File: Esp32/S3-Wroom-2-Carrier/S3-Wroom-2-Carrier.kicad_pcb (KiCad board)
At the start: 6 copper layers, 3 parts, among them J1 DF9-21S-1V32, J2 DF9-21S-1V32

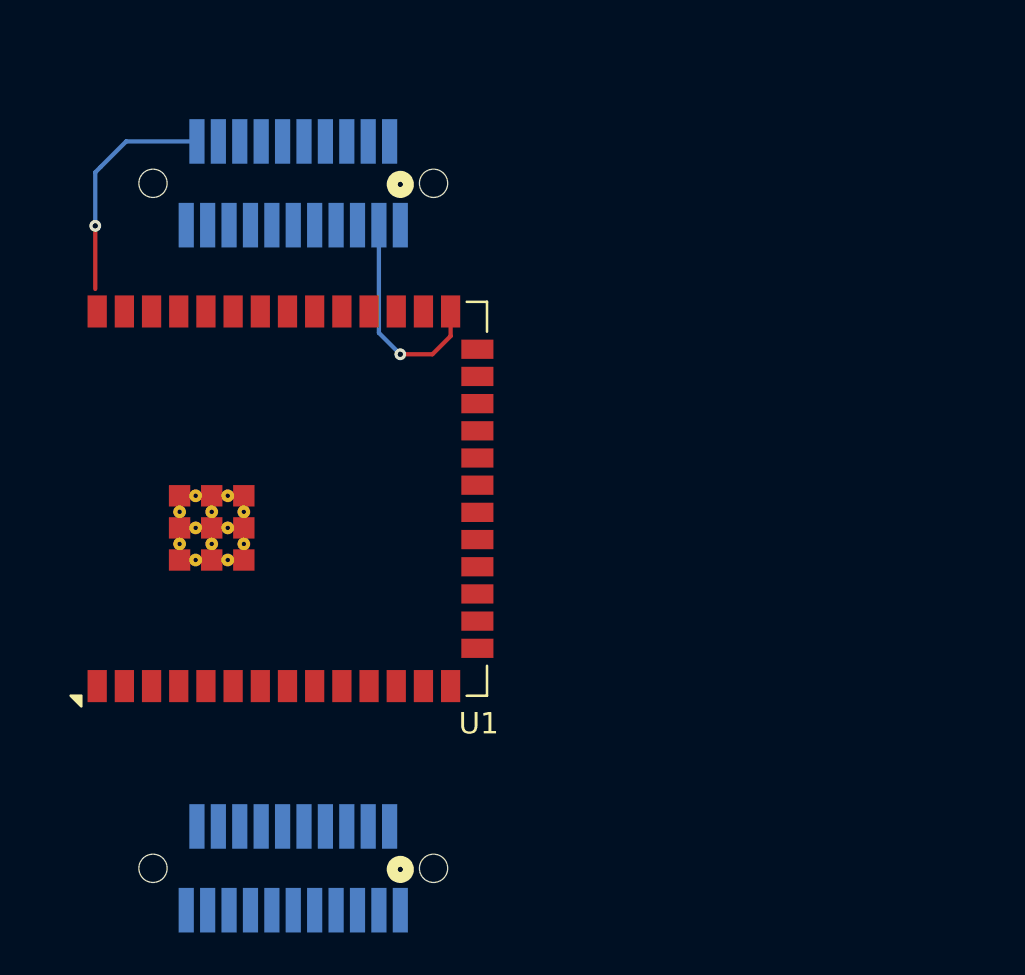
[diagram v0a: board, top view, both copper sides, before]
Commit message: Power sheet
Added Esp32 power sheet and rename previous sheets
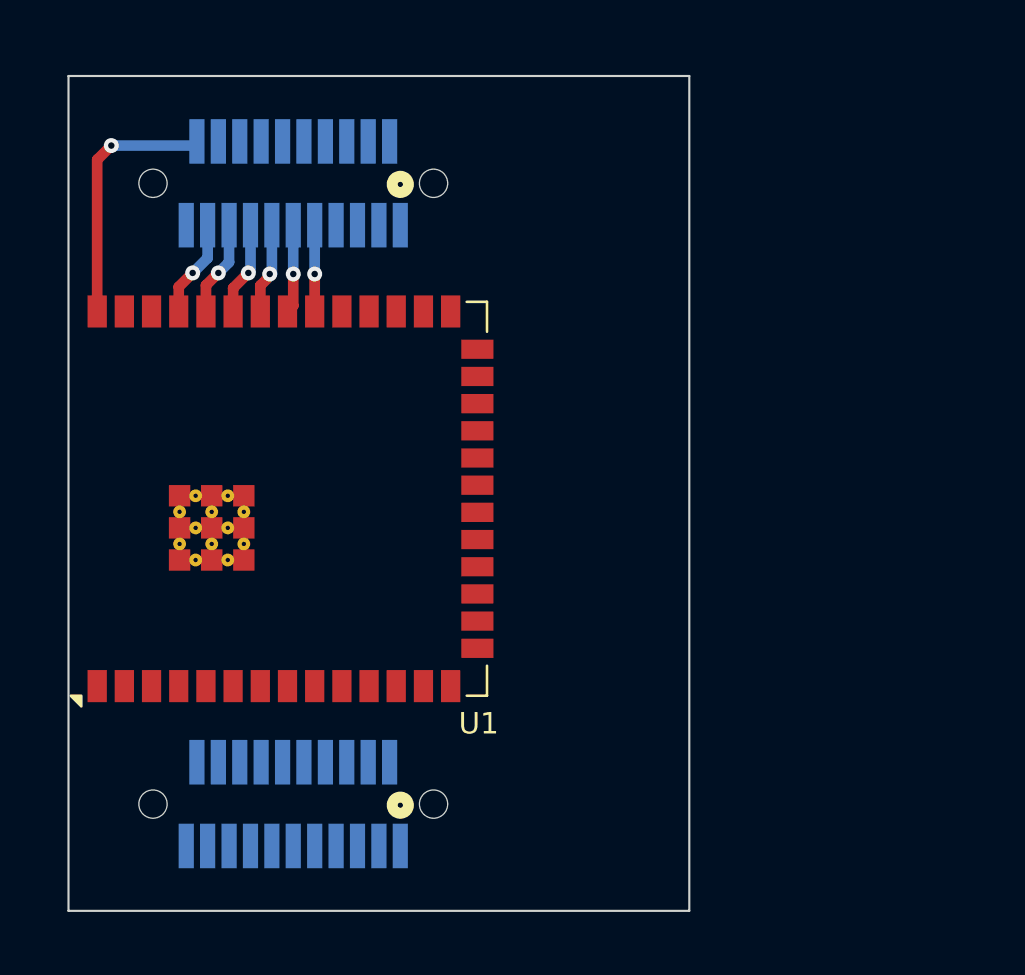
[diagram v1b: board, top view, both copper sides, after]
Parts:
- moved J2 3.00 mm to (146.5, 114.0)
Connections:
- J1 pad 11: unconnected-(J1-Pad11) -> /Project Architecture/Section A - Title A/JTAG.TDO
- J1 pad 13: unconnected-(J1-Pad13) -> /Project Architecture/Section A - Title A/JTAG.TDI
- J1 pad 15: unconnected-(J1-Pad15) -> /Project Architecture/Section A - Title A/JTAG.TMS
- J1 pad 17: unconnected-(J1-Pad17) -> /Project Architecture/Section A - Title A/RXDO
- J1 pad 19: unconnected-(J1-Pad19) -> /Project Architecture/Section A - Title A/TXDO
- J1 pad 20: unconnected-(J1-Pad20) -> GND
- J1 pad 3: /Project Architecture/Section A - Title A/GPIO0 -> unconnected-(J1-Pad3)
- J1 pad 4: /Project Architecture/Section A - Title A/GPIO1 -> unconnected-(J1-Pad4)
- J1 pad 5: /Project Architecture/Section A - Title A/GPIO2 -> unconnected-(J1-Pad5)
- J1 pad 6: /Project Architecture/Section A - Title A/GPIO3 -> unconnected-(J1-Pad6)
- J1 pad 7: /Project Architecture/Section A - Title A/GPIO4 -> unconnected-(J1-Pad7)
- J1 pad 8: /Project Architecture/Section A - Title A/GPIO5 -> unconnected-(J1-Pad8)
- J1 pad 9: unconnected-(J1-Pad9) -> /Project Architecture/Section A - Title A/JTAG.TCLK
- J2 pad 2: unconnected-(J2-Pad2) -> /Project Architecture/Section A - Title A/USB_D+
- J2 pad 20: unconnected-(J2-Pad20) -> /Project Architecture/Section A - Title A/EN
- J2 pad 21: unconnected-(J2-Pad21) -> +3V3
- J2 pad 4: unconnected-(J2-Pad4) -> /Project Architecture/Section A - Title A/USB_D-
- U1 pad 1: (no net) -> GND
- U1 pad 13: /Project Architecture/Section A - Title A/US_D- -> /Project Architecture/Section A - Title A/USB_D-
- U1 pad 28: (no net) -> unconnected-(U1C-NC-Pad28)
- U1 pad 29: (no net) -> unconnected-(U1C-NC-Pad29)
- U1 pad 3: EN -> /Project Architecture/Section A - Title A/EN
- U1 pad 30: (no net) -> unconnected-(U1C-NC-Pad30)
- U1 pad 40: (no net) -> GND
- U1 pad 41: (no net) -> GND
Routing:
- net GND: track 0.00 -> 12.1 mm, vias 0 -> 1
- net unconnected-(J1-Pad20): track 10.8 -> 0.00 mm, vias 1 -> 0
- net /Project Architecture/Section A - Title A/GPIO0: track 10.3 -> 0.00 mm, vias 1 -> 0
- net /Project Architecture/Section A - Title A/TXDO: track 0.00 -> 4.59 mm, vias 0 -> 1
- net /Project Architecture/Section A - Title A/RXDO: track 0.00 -> 4.48 mm, vias 0 -> 1
- net /Project Architecture/Section A - Title A/JTAG.TMS: track 0.00 -> 4.45 mm, vias 0 -> 1
- net /Project Architecture/Section A - Title A/JTAG.TDI: track 0.00 -> 4.26 mm, vias 0 -> 1
- net /Project Architecture/Section A - Title A/JTAG.TCLK: track 0.00 -> 4.03 mm, vias 0 -> 1
- net /Project Architecture/Section A - Title A/JTAG.TDO: track 0.00 -> 3.89 mm, vias 0 -> 1
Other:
- board outline added: 29 x 39 mm

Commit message: Connectors
Lower connector routed
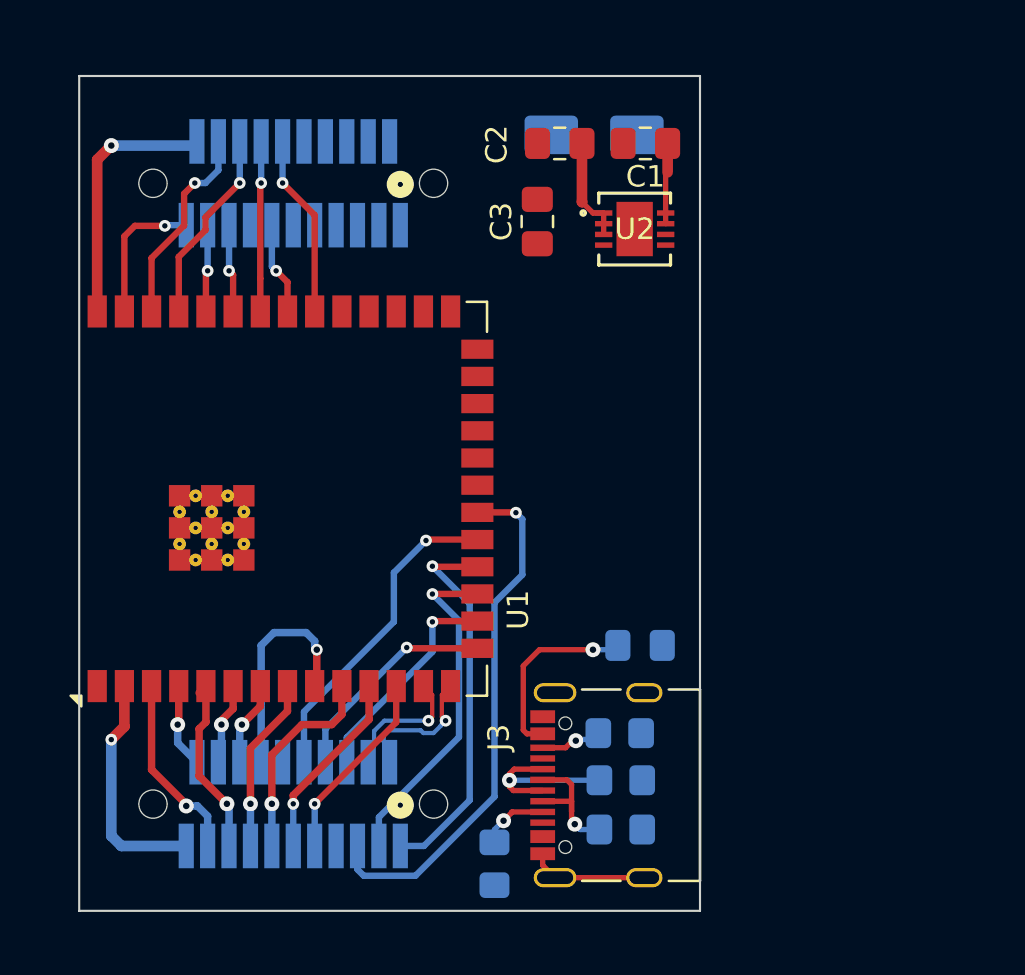
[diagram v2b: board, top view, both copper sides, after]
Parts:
- added C1: 4u7F, Capacitor_SMD:C_0805_2012Metric_Pad1.18x1.45mm_HandSolder, F.Cu at (162.9, 83.2)
- added C2: 4u7F, Capacitor_SMD:C_0805_2012Metric_Pad1.18x1.45mm_HandSolder, F.Cu at (158.9, 83.2)
- added C3: 1nF, Capacitor_SMD:C_0805_2012Metric_Pad1.18x1.45mm_HandSolder, F.Cu at (157.9, 86.8)
- added C4: 1uF, Capacitor_SMD:C_0805_2012Metric_Pad1.18x1.45mm_HandSolder, B.Cu at (162.7, 106.6)
- added D2: B340, Diode_SMD:D_SMA, B.Cu at (160.6, 82.7)
- added J3: USB_C_Receptacle_USB2.0_16P, Connector_USB:USB_C_Receptacle_Palconn_UTC16-G, F.Cu at (160.7, 113.1)
- added R1: 22, Resistor_SMD:R_0805_2012Metric_Pad1.20x1.40mm_HandSolder, B.Cu at (161.8, 115.2)
- added R2: 22, Resistor_SMD:R_0805_2012Metric_Pad1.20x1.40mm_HandSolder, B.Cu at (161.8, 112.9)
- added R3: 5K1, Resistor_SMD:R_0805_2012Metric_Pad1.20x1.40mm_HandSolder, B.Cu at (155.9, 116.8)
- added R4: 5K1, Resistor_SMD:R_0805_2012Metric_Pad1.20x1.40mm_HandSolder, B.Cu at (161.8, 110.7)
- added U2: ADM7171ACPZ-3.0-R7, User_Footprint:LFCSP-8-1EP_3x3mm_P0.5mm_EP_1.70x2.54mm, F.Cu at (162.4, 87.2)
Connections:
- net /Project Architecture/Section A - Title A/GPIO13 renamed /Project Architecture/Break Out Connection/GPIO13
- net /Project Architecture/Section A - Title A/GPIO14 renamed /Project Architecture/Break Out Connection/GPIO14
- net /Project Architecture/Section A - Title A/GPIO21 renamed /Project Architecture/Break Out Connection/GPIO21
- net /Project Architecture/Section A - Title A/GPIO47 renamed /Project Architecture/Break Out Connection/GPIO47
- net /Project Architecture/Section A - Title A/USB_D+ renamed /Project Architecture/Break Out Connection/USB_D+
- net /Project Architecture/Section A - Title A/USB_D- renamed /Project Architecture/Break Out Connection/USB_D-
- J1 pad 1: unconnected-(J1-Pad1) -> /Project Architecture/Break Out Connection/GPIO0
- J1 pad 11: /Project Architecture/Section A - Title A/JTAG.TDO -> unconnected-(J1-Pad11)
- J1 pad 12: unconnected-(J1-Pad12) -> /Project Architecture/Break Out Connection/JTAG.TCLK
- J1 pad 13: /Project Architecture/Section A - Title A/JTAG.TDI -> /Project Architecture/Break Out Connection/JTAG.TDO
- J1 pad 14: unconnected-(J1-Pad14) -> /Project Architecture/Break Out Connection/JTAG.TDI
- J1 pad 15: /Project Architecture/Section A - Title A/JTAG.TMS -> GND
- J1 pad 16: unconnected-(J1-Pad16) -> /Project Architecture/Break Out Connection/TXDO
- J1 pad 17: /Project Architecture/Section A - Title A/RXDO -> /Project Architecture/Break Out Connection/JTAG.TMS
- J1 pad 18: unconnected-(J1-Pad18) -> /Project Architecture/Break Out Connection/GPIO2
- J1 pad 19: /Project Architecture/Section A - Title A/TXDO -> /Project Architecture/Break Out Connection/RXDO
- J1 pad 21: unconnected-(J1-Pad21) -> /Project Architecture/Break Out Connection/GPIO1
- J1 pad 3: unconnected-(J1-Pad3) -> /Project Architecture/Break Out Connection/GPIO45
- J1 pad 5: unconnected-(J1-Pad5) -> /Project Architecture/Break Out Connection/GPIO48
- J1 pad 7: unconnected-(J1-Pad7) -> /Project Architecture/Break Out Connection/GPIO38
- J1 pad 9: /Project Architecture/Section A - Title A/JTAG.TCLK -> unconnected-(J1-Pad9)
- J2 pad 1: unconnected-(J2-Pad1) -> /Project Architecture/Break Out Connection/GPIO10
- J2 pad 10: unconnected-(J2-Pad10) -> /Project Architecture/Break Out Connection/GPIO11
- J2 pad 11: unconnected-(J2-Pad11) -> /Project Architecture/Break Out Connection/GPIO18
- J2 pad 12: unconnected-(J2-Pad12) -> /Project Architecture/Break Out Connection/GPIO7
- J2 pad 13: unconnected-(J2-Pad13) -> /Project Architecture/Break Out Connection/GPIO17
- J2 pad 14: unconnected-(J2-Pad14) -> /Project Architecture/Break Out Connection/GPIO16
- J2 pad 15: unconnected-(J2-Pad15) -> /Project Architecture/Break Out Connection/GPIO15
- J2 pad 16: unconnected-(J2-Pad16) -> /Project Architecture/Break Out Connection/GPIO7
- J2 pad 17: unconnected-(J2-Pad17) -> /Project Architecture/Break Out Connection/GPIO5
- J2 pad 18: unconnected-(J2-Pad18) -> /Project Architecture/Break Out Connection/GPIO6
- J2 pad 19: unconnected-(J2-Pad19) -> /Project Architecture/EN
- J2 pad 20: /Project Architecture/Section A - Title A/EN -> /Project Architecture/Break Out Connection/GPIO4
- J2 pad 3: unconnected-(J2-Pad3) -> /Project Architecture/Break Out Connection/GPIO9
- J2 pad 5: unconnected-(J2-Pad5) -> /Project Architecture/Break Out Connection/GPIO12
- J2 pad 6: unconnected-(J2-Pad6) -> /Project Architecture/Break Out Connection/GPIO46
- J2 pad 7: unconnected-(J2-Pad7) -> GND
- J2 pad 8: unconnected-(J2-Pad8) -> /Project Architecture/Break Out Connection/GPIO3
- J2 pad 9: unconnected-(J2-Pad9) -> /Project Architecture/Break Out Connection/GPIO8
- U1 pad 10: /Project Architecture/Section A - Title A/GPIO17 -> /Project Architecture/Break Out Connection/GPIO17
- U1 pad 11: /Project Architecture/Section A - Title A/GPIO18 -> /Project Architecture/Break Out Connection/GPIO18
- U1 pad 12: /Project Architecture/Section A - Title A/GPIO8 -> /Project Architecture/Break Out Connection/GPIO8
- U1 pad 15: /Project Architecture/Section A - Title A/GPIO3 -> /Project Architecture/Break Out Connection/GPIO3
- U1 pad 16: /Project Architecture/Section A - Title A/GPIO46 -> /Project Architecture/Break Out Connection/GPIO46
- U1 pad 17: /Project Architecture/Section A - Title A/GPIO9 -> /Project Architecture/Break Out Connection/GPIO9
- U1 pad 18: /Project Architecture/Section A - Title A/GPIO10 -> /Project Architecture/Break Out Connection/GPIO10
- U1 pad 19: /Project Architecture/Section A - Title A/GPIO11 -> /Project Architecture/Break Out Connection/GPIO11
- U1 pad 20: /Project Architecture/Section A - Title A/GPIO12 -> /Project Architecture/Break Out Connection/GPIO12
- U1 pad 25: /Project Architecture/Section A - Title A/GPIO48 -> /Project Architecture/Break Out Connection/GPIO48
- U1 pad 26: /Project Architecture/Section A - Title A/GPIO45 -> /Project Architecture/Break Out Connection/GPIO45
- U1 pad 27: /Project Architecture/Section A - Title A/GPIO0 -> /Project Architecture/Break Out Connection/GPIO0
- U1 pad 3: /Project Architecture/Section A - Title A/EN -> /Project Architecture/EN
- U1 pad 31: /Project Architecture/Section A - Title A/GPIO38 -> /Project Architecture/Break Out Connection/GPIO38
- U1 pad 32: /Project Architecture/Section A - Title A/JTAG.TCLK -> /Project Architecture/Break Out Connection/JTAG.TCLK
- U1 pad 33: /Project Architecture/Section A - Title A/JTAG.TDO -> /Project Architecture/Break Out Connection/JTAG.TDO
- U1 pad 34: /Project Architecture/Section A - Title A/JTAG.TDI -> /Project Architecture/Break Out Connection/JTAG.TDI
- U1 pad 35: /Project Architecture/Section A - Title A/JTAG.TMS -> /Project Architecture/Break Out Connection/JTAG.TMS
- U1 pad 36: /Project Architecture/Section A - Title A/RXDO -> /Project Architecture/Break Out Connection/RXDO
- U1 pad 37: /Project Architecture/Section A - Title A/TXDO -> /Project Architecture/Break Out Connection/TXDO
- U1 pad 38: /Project Architecture/Section A - Title A/GPIO2 -> /Project Architecture/Break Out Connection/GPIO2
- U1 pad 39: /Project Architecture/Section A - Title A/GPIO1 -> /Project Architecture/Break Out Connection/GPIO1
- U1 pad 4: /Project Architecture/Section A - Title A/GPIO4 -> /Project Architecture/Break Out Connection/GPIO4
- U1 pad 5: /Project Architecture/Section A - Title A/GPIO5 -> /Project Architecture/Break Out Connection/GPIO5
- U1 pad 6: /Project Architecture/Section A - Title A/GPIO6 -> /Project Architecture/Break Out Connection/GPIO6
- U1 pad 7: /Project Architecture/Section A - Title A/GPIO7 -> /Project Architecture/Break Out Connection/GPIO7
- U1 pad 8: /Project Architecture/Section A - Title A/GPIO15 -> /Project Architecture/Break Out Connection/GPIO15
- U1 pad 9: /Project Architecture/Section A - Title A/GPIO16 -> /Project Architecture/Break Out Connection/GPIO16
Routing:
- net /Project Architecture/Break Out Connection/GPIO12: track 0.00 -> 24.9 mm, vias 0 -> 1
- net /Project Architecture/Break Out Connection/GPIO10: track 0.00 -> 17.9 mm, vias 0 -> 1
- net +3V3: track 0.00 -> 16.1 mm, vias 0 -> 1
- net /Project Architecture/Break Out Connection/GPIO9: track 0.00 -> 15.9 mm, vias 0 -> 1
- net /Project Architecture/Break Out Connection/GPIO11: track 0.00 -> 15.1 mm, vias 0 -> 1
- net /Project Architecture/Break Out Connection/GPIO16: track 0.00 -> 10.6 mm, vias 0 -> 1
- net /Project Architecture/Break Out Connection/GPIO46: track 0.00 -> 10.3 mm, vias 0 -> 1
- net /Project Architecture/Break Out Connection/GPIO3: track 0.00 -> 10.2 mm, vias 0 -> 1
- net /Project Architecture/Break Out Connection/GPIO17: track 0.00 -> 9.64 mm, vias 0 -> 1
- net /Project Architecture/Break Out Connection/GPIO2: track 0.00 -> 9.53 mm, vias 0 -> 1
- net /Project Architecture/Break Out Connection/TXDO: track 0.00 -> 9.12 mm, vias 0 -> 1
- net /Project Architecture/Break Out Connection/GPIO8: track 0.00 -> 9.05 mm, vias 0 -> 1
- net /Project Architecture/Break Out Connection/GPIO18: track 0.00 -> 8.93 mm, vias 0 -> 1
- net /Project Architecture/EN: track 0.00 -> 8.86 mm, vias 0 -> 1
- net Net-(D2-A): track 0.00 -> 8.79 mm, vias 0 -> 1
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
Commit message: Routing
Routing finished needs to be verify
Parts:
- removed J1: DF9-21S-1V32, Library:CON9_1X21_DZL_DF9_HIR
- removed J3: USB_C_Receptacle_USB2.0_16P, Connector_USB:USB_C_Receptacle_Palconn_UTC16-G
- removed R4: 5K1, Resistor_SMD:R_0805_2012Metric_Pad1.20x1.40mm_HandSolder
- added D1: ~, User_Footprint:DIOC1608X36N, F.Cu at (159.4, 108.4)
- added D3: ~, User_Footprint:DIOC1608X36N, F.Cu at (159.5, 116.0)
- added J4: DF9B-21S-1V69, User_Footprint:CONN_DF9B-21S-1V_21P_HIR, B.Cu at (146.4, 113.8)
- added J5: DF9B-21S-1V69, User_Footprint:CONN_DF9B-21S-1V_21P_HIR, B.Cu at (146.4, 85.0)
- added R5: 10K, Resistor_SMD:R_0805_2012Metric_Pad1.20x1.40mm_HandSolder, B.Cu at (142.5, 106.4)
- added R6: 10K, Resistor_SMD:R_0805_2012Metric_Pad1.20x1.40mm_HandSolder, B.Cu at (155.4, 94.7)
- J2: value DF9-21S-1V32 -> 65100516121; footprint Library:CON9_1X21_DZL_DF9_HIR -> User_Footprint:Usb_B_mini_Wurth_65100516121; moved to F.Cu
- R1, R2: moved to F.Cu
- moved D2 20.3 mm to (167.9, 101.7), turned to -90 degrees
- moved J2 19.9 mm to (166.2, 111.6), turned to 90 degrees
- moved C2 15.7 mm to (160.4, 98.8), turned to -90 degrees
- moved C3 15.2 mm to (163.8, 100.8), turned to 0 degrees
- moved C1 11.2 mm to (164.6, 94.2)
- moved U2 10.5 mm to (164.2, 97.6)
- moved R2 4.61 mm to (157.6, 111.0), turned to 0 degrees
- moved R1 4.57 mm to (157.6, 113.4), turned to 0 degrees
- moved R3 3.80 mm to (157.6, 113.4), turned to 0 degrees
- moved C4 2.77 mm to (164.2, 104.2), turned to 180 degrees
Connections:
- C4 pad 1: Net-(D2-A) -> /Project Architecture/Power/VBUS
- D2 pad 2: Net-(D2-A) -> /Project Architecture/Power/VBUS
- J2 pad 1: /Project Architecture/Break Out Connection/GPIO10 -> /Project Architecture/Power/VBUS
- J2 pad 2: /Project Architecture/Break Out Connection/USB_D+ -> Net-(J2-D-)
- J2 pad 3: /Project Architecture/Break Out Connection/GPIO9 -> Net-(J2-D+)
- J2 pad 4: /Project Architecture/Break Out Connection/USB_D- -> unconnected-(J2-ID-Pad4)
- J2 pad 5: /Project Architecture/Break Out Connection/GPIO12 -> GND
- R1 pad 2: Net-(J3-D--PadA7) -> Net-(J2-D-)
- R2 pad 2: Net-(J3-D+-PadA6) -> Net-(J2-D+)
- U1 pad 28: unconnected-(U1C-NC-Pad28) -> /Project Architecture/Break Out Connection/GPIO35
- U1 pad 29: unconnected-(U1C-NC-Pad29) -> /Project Architecture/Break Out Connection/GPIO36
- U1 pad 30: unconnected-(U1C-NC-Pad30) -> /Project Architecture/Break Out Connection/GPIO37
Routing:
- net /Project Architecture/Break Out Connection/GPIO14: track 0.00 -> 34.4 mm, vias 0 -> 1
- net +3V3: track 16.1 -> 47.7 mm, vias 1 -> 4
- net /Project Architecture/Break Out Connection/GPIO47: track 0.00 -> 28.8 mm, vias 0 -> 1
- net /Project Architecture/Break Out Connection/GPIO21: track 0.00 -> 26.6 mm, vias 0 -> 1
- net /Project Architecture/Break Out Connection/GPIO13: track 0.00 -> 23.7 mm, vias 0 -> 1
- net GND: track 17.6 -> 38.3 mm, vias 1 -> 12
- net /Project Architecture/Power/VBUS: track 0.00 -> 20.5 mm, vias 0 -> 1
- net /Project Architecture/Break Out Connection/GPIO48: track 0.00 -> 10.7 mm, vias 0 -> 1
- net /Project Architecture/Break Out Connection/GPIO37: track 0.00 -> 9.97 mm, vias 0 -> 1
- net /Project Architecture/Break Out Connection/GPIO35: track 0.00 -> 9.60 mm, vias 0 -> 1
- net /Project Architecture/Break Out Connection/GPIO36: track 0.00 -> 9.47 mm, vias 0 -> 1
- net /Project Architecture/Break Out Connection/GPIO0: track 0.00 -> 9.34 mm, vias 0 -> 2
- net /Project Architecture/Break Out Connection/GPIO45: track 0.00 -> 9.13 mm, vias 0 -> 1
- net Net-(D2-A): track 8.79 -> 0.00 mm, vias 1 -> 0
- net /Project Architecture/Break Out Connection/GPIO9: track 15.9 -> 24.4 mm
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- added copper zone on B.Cu, net GND
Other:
- board size 29 x 39 mm -> 35.8 x 39.4 mm
- copper layers 6 -> 2
